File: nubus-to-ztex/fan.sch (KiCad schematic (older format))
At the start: 6 parts, among them J10 Conn_01x03_Male, J7 Conn_01x03_Male, J9 Conn_01x02

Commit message: large update
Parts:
- removed C33: 10uF, Capacitor_SMD:C_0805_2012Metric, symbol Device:C
- removed J10: Conn_01x03_Male, Connector_Molex:Molex_KK-254_AE-6410-03A_1x03_P2.54mm_Vertical, symbol Connector:Conn_01x03_Male
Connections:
- net labels removed: +12V
- wire segments 12 -> 8
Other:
- note removed: "12V Fan"
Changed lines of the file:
@@
 $Descr A4 11693 8268
 encoding utf-8
-Sheet 7 7
+Sheet 6 7
 Title "sbus-to-ztex blinkey stuff"
 Date ""
@@
 	6600 4500 6200 4500
 Connection ~ 6600 4400
-$Comp
-L Connector:Conn_01x03_Male J10
-U 1 1 61C52A59
-P 4400 5800
-F 0 "J10" H 4506 6078 50  0000 C CNN
-F 1 "Conn_01x03_Male" H 4506 5987 50  0000 C CNN
-F 2 "Connector_Molex:Molex_KK-254_AE-6410-03A_1x03_P2.54mm_Vertical" H 4400 5800 50  0001 C CNN
-F 3 "~" H 4400 5800 50  0001 C CNN
-F 4 "22-27-2031" H 4400 5800 50  0001 C CNN "MPN-ALT"
-F 5 "Molex" H 4400 5800 50  0001 C CNN "Manufacturer-ALT"
-F 6 "https://www.mouser.fr/ProductDetail/Molex/22-27-2031?qs=%2Fha2pyFadugXOaGYK9vaczm7nZ04txhJn3OGcnGWT3U=" H 4400 5800 50  0001 C CNN "URL-ALT"
-F 7 "640456-3" H 4400 5800 50  0001 C CNN "MPN"
-F 8 "TE Connectivity" H 4400 5800 50  0001 C CNN "Manufacturer"
-F 9 "https://www.lcsc.com/product-detail/Wire-To-Board-Wire-To-Wire-Connector_TE-Connectivity-640456-3_C86503.html" H 4400 5800 50  0001 C CNN "URL"
-	1    4400 5800
-	1    0    0    -1
-$EndComp
-$Comp
-L power:GND #PWR0208
-U 1 1 61C52A60
-P 4600 5700
-F 0 "#PWR0208" H 4600 5450 50  0001 C CNN
-F 1 "GND" V 4605 5572 50  0000 R CNN
-F 2 "" H 4600 5700 50  0001 C CNN
-F 3 "" H 4600 5700 50  0001 C CNN
-	1    4600 5700
-	0    -1   -1   0
-$EndComp
-$Comp
-L power:GND #PWR0209
-U 1 1 61C52A6C
-P 4600 5900
-F 0 "#PWR0209" H 4600 5650 50  0001 C CNN
-F 1 "GND" V 4605 5772 50  0000 R CNN
-F 2 "" H 4600 5900 50  0001 C CNN
-F 3 "" H 4600 5900 50  0001 C CNN
-	1    4600 5900
-	0    -1   -1   0
-$EndComp
-$Comp
-L Device:C C?
-U 1 1 61C52A73
-P 5150 5850
-AR Path="/5F69F4EF/61C52A73" Ref="C?"  Part="1"
-AR Path="/5F6B165A/61C52A73" Ref="C?"  Part="1"
-AR Path="/61B99D2C/61C52A73" Ref="C33"  Part="1"
-F 0 "C33" H 5175 5950 50  0000 L CNN
-F 1 "10uF" H 5175 5750 50  0000 L CNN
-F 2 "Capacitor_SMD:C_0805_2012Metric" H 5188 5700 50  0001 C CNN
-F 3 "" H 5150 5850 50  0000 C CNN
-F 4 "GRM21BR61E106MA73L" H 5150 5850 50  0001 C CNN "MPN"
-F 5 "https://lcsc.com/product-detail/Multilayer-Ceramic-Capacitors-MLCC-SMD-SMT_Murata-Electronics-GRM21BR61E106MA73L_C391262.html" H 5150 5850 50  0001 C CNN "URL"
-	1    5150 5850
-	1    0    0    -1
-$EndComp
-Wire Wire Line
-	4600 5800 5150 5800
-Wire Wire Line
-	5150 5800 5150 5700
-Wire Wire Line
-	4600 5900 5150 5900
-Wire Wire Line
-	5150 5900 5150 6000
-Connection ~ 4600 5900
-$Comp
-L power:+12V #PWR0210
-U 1 1 61C52B88
-P 4600 5800
-F 0 "#PWR0210" H 4600 5650 50  0001 C CNN
-F 1 "+12V" V 4615 5928 50  0000 L CNN
-F 2 "" H 4600 5800 50  0001 C CNN
-F 3 "" H 4600 5800 50  0001 C CNN
-	1    4600 5800
-	0    1    1    0
-$EndComp
-Connection ~ 4600 5800
 Text Notes 3950 4750 0    50   ~ 0
 5V Fan
-Text Notes 4000 5850 0    50   ~ 0
-12V Fan
 Text Notes 6800 4600 0    50   ~ 0
 3.3V access

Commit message: large clean-up update
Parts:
- renumbered C6 to C28, C31 to C29, J9 to J8
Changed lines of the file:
@@
 encoding utf-8
 Sheet 6 7
-Title "sbus-to-ztex blinkey stuff"
+Title "nubus-to-ztex extra conenctors (fan, ...)"
 Date ""
 Rev ""
@@
 $EndComp
 $Comp
-L power:GND #PWR0187
+L power:GND #PWR0107
 U 1 1 60E1EC2C
 P 4600 4650
-F 0 "#PWR0187" H 4600 4400 50  0001 C CNN
+F 0 "#PWR0107" H 4600 4400 50  0001 C CNN
 F 1 "GND" V 4605 4522 50  0000 R CNN
 F 2 "" H 4600 4650 50  0001 C CNN
@@
 $EndComp
 $Comp
-L power:+5V #PWR0188
+L power:+5V #PWR0108
 U 1 1 60E1ED6C
 P 4600 4750
-F 0 "#PWR0188" H 4600 4600 50  0001 C CNN
+F 0 "#PWR0108" H 4600 4600 50  0001 C CNN
 F 1 "+5V" V 4615 4878 50  0000 L CNN
 F 2 "" H 4600 4750 50  0001 C CNN
@@
 $EndComp
 $Comp
-L power:GND #PWR0189
+L power:GND #PWR0109
 U 1 1 60E1FA97
 P 4600 4850
-F 0 "#PWR0189" H 4600 4600 50  0001 C CNN
+F 0 "#PWR0109" H 4600 4600 50  0001 C CNN
 F 1 "GND" V 4605 4722 50  0000 R CNN
 F 2 "" H 4600 4850 50  0001 C CNN
@@
 P 5150 4800
 AR Path="/5F69F4EF/60E24715" Ref="C?"  Part="1"
-AR Path="/5F6B165A/60E24715" Ref="C6"  Part="1"
-AR Path="/61B99D2C/60E24715" Ref="C20"  Part="1"
-F 0 "C20" H 5175 4900 50  0000 L CNN
+AR Path="/5F6B165A/60E24715" Ref="C?"  Part="1"
+AR Path="/61B99D2C/60E24715" Ref="C28"  Part="1"
+F 0 "C28" H 5175 4900 50  0000 L CNN
 F 1 "47uF 10V+" H 5175 4700 50  0000 L CNN
 F 2 "Capacitor_SMD:C_0805_2012Metric" H 5188 4650 50  0001 C CNN
@@
 Connection ~ 4600 4850
 $Comp
-L Connector_Generic:Conn_01x02 J9
+L Connector_Generic:Conn_01x02 J8
 U 1 1 61BEF34E
 P 6800 4300
-F 0 "J9" H 6880 4292 50  0000 L CNN
+F 0 "J8" H 6880 4292 50  0000 L CNN
 F 1 "Conn_01x02" H 6880 4201 50  0000 L CNN
 F 2 "For_SeeedStudio:PinSocket_1x02_P2.54mm_Vertical_for_SeeedStudio" H 6800 4300 50  0001 C CNN
@@
 $EndComp
 $Comp
-L power:+3V3 #PWR0102
+L power:+3V3 #PWR0110
 U 1 1 61BEF445
 P 6600 4300
-F 0 "#PWR0102" H 6600 4150 50  0001 C CNN
+F 0 "#PWR0110" H 6600 4150 50  0001 C CNN
 F 1 "+3V3" V 6615 4428 50  0000 L CNN
 F 2 "" H 6600 4300 50  0001 C CNN
@@
 $EndComp
 $Comp
-L power:GND #PWR0200
+L power:GND #PWR0111
 U 1 1 61BEF4B8
 P 6600 4400
-F 0 "#PWR0200" H 6600 4150 50  0001 C CNN
+F 0 "#PWR0111" H 6600 4150 50  0001 C CNN
 F 1 "GND" V 6605 4272 50  0000 R CNN
 F 2 "" H 6600 4400 50  0001 C CNN
@@
 AR Path="/5F69F4EF/61C19258" Ref="C?"  Part="1"
 AR Path="/5F6B165A/61C19258" Ref="C?"  Part="1"
-AR Path="/61B99D2C/61C19258" Ref="C31"  Part="1"
-F 0 "C31" H 6225 4450 50  0000 L CNN
+AR Path="/61B99D2C/61C19258" Ref="C29"  Part="1"
+F 0 "C29" H 6225 4450 50  0000 L CNN
 F 1 "47uF 10V+" H 6225 4250 50  0000 L CNN
 F 2 "Capacitor_SMD:C_0805_2012Metric" H 6238 4200 50  0001 C CNN

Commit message: cut down brightness of LEDs, more 2x32 pin headers reference
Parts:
- removed C29: 47uF 10V+, Capacitor_SMD:C_0805_2012Metric, symbol Device:C
- removed J8: Conn_01x02, For_SeeedStudio:PinSocket_1x02_P2.54mm_Vertical_for_SeeedStudio, symbol Connector_Generic:Conn_01x02
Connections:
- net labels removed: +3V3
- wire segments 8 -> 4
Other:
- note removed: "3.3V access"
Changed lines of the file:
@@
 $Descr A4 11693 8268
 encoding utf-8
-Sheet 6 9
+Sheet 6 10
 Title "nubus-to-ztex extra conenctors (fan, ...)"
 Date ""
@@
 	5150 4850 5150 4950
 Connection ~ 4600 4850
-$Comp
-L Connector_Generic:Conn_01x02 J8
-U 1 1 61BEF34E
-P 6800 4300
-F 0 "J8" H 6880 4292 50  0000 L CNN
-F 1 "Conn_01x02" H 6880 4201 50  0000 L CNN
-F 2 "For_SeeedStudio:PinSocket_1x02_P2.54mm_Vertical_for_SeeedStudio" H 6800 4300 50  0001 C CNN
-F 3 "~" H 6800 4300 50  0001 C CNN
-F 4 "PM254V-11-02-H85" H 6800 4300 50  0001 C CNN "MPN"
-F 5 "https://www.lcsc.com/product-detail/Pin-Header-Female-Header_XFCN-PM254V-11-02-H85_C541849.html" H 6800 4300 50  0001 C CNN "URL"
-	1    6800 4300
-	1    0    0    -1
-$EndComp
-$Comp
-L power:+3V3 #PWR0110
-U 1 1 61BEF445
-P 6600 4300
-F 0 "#PWR0110" H 6600 4150 50  0001 C CNN
-F 1 "+3V3" V 6615 4428 50  0000 L CNN
-F 2 "" H 6600 4300 50  0001 C CNN
-F 3 "" H 6600 4300 50  0001 C CNN
-	1    6600 4300
-	0    -1   -1   0
-$EndComp
-$Comp
-L power:GND #PWR0111
-U 1 1 61BEF4B8
-P 6600 4400
-F 0 "#PWR0111" H 6600 4150 50  0001 C CNN
-F 1 "GND" V 6605 4272 50  0000 R CNN
-F 2 "" H 6600 4400 50  0001 C CNN
-F 3 "" H 6600 4400 50  0001 C CNN
-	1    6600 4400
-	0    1    1    0
-$EndComp
-$Comp
-L Device:C C?
-U 1 1 61C19258
-P 6200 4350
-AR Path="/5F69F4EF/61C19258" Ref="C?"  Part="1"
-AR Path="/5F6B165A/61C19258" Ref="C?"  Part="1"
-AR Path="/61B99D2C/61C19258" Ref="C29"  Part="1"
-F 0 "C29" H 6225 4450 50  0000 L CNN
-F 1 "47uF 10V+" H 6225 4250 50  0000 L CNN
-F 2 "Capacitor_SMD:C_0805_2012Metric" H 6238 4200 50  0001 C CNN
-F 3 "" H 6200 4350 50  0000 C CNN
-F 4 "C2012X5R1A476MTJ00E" H 6200 4350 50  0001 C CNN "MPN"
-F 5 "https://lcsc.com/product-detail/Multilayer-Ceramic-Capacitors-MLCC-SMD-SMT_TDK-C2012X5R1A476MTJ00E_C76636.html" H 6200 4350 50  0001 C CNN "URL"
-	1    6200 4350
-	1    0    0    -1
-$EndComp
-Wire Wire Line
-	6200 4200 6600 4200
-Wire Wire Line
-	6600 4200 6600 4300
-Connection ~ 6600 4300
-Wire Wire Line
-	6600 4400 6600 4500
-Wire Wire Line
-	6600 4500 6200 4500
-Connection ~ 6600 4400
 Text Notes 3950 4750 0    50   ~ 0
 5V Fan
-Text Notes 6800 4600 0    50   ~ 0
-3.3V access
 $EndSCHEMATC

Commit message: merge pmod & leds into an extended pmod on the outside. Also some BoM updates.
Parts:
- C28: MPN C2012X5R1A476MTJ00E -> GRM21BR61A476ME15K; MPN-ALT (none) -> C2012X5R1A476MTJ00E; URL https://lcsc.com/product-detail/Multilayer-Ceramic-Capacito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 -> https://www.lcsc.com/product-detail/Multilayer-Ceramic-Capa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; URL-ALT (none) -> https://lcsc.com/product-detail/Multilayer-Ceramic-Capacito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
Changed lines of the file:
@@
 $Descr A4 11693 8268
 encoding utf-8
-Sheet 6 10
+Sheet 6 9
 Title "nubus-to-ztex extra conenctors (fan, ...)"
 Date ""
@@
 F 2 "Capacitor_SMD:C_0805_2012Metric" H 5188 4650 50  0001 C CNN
 F 3 "" H 5150 4800 50  0000 C CNN
-F 4 "C2012X5R1A476MTJ00E" H 5150 4800 50  0001 C CNN "MPN"
-F 5 "https://lcsc.com/product-detail/Multilayer-Ceramic-Capacitors-MLCC-SMD-SMT_TDK-C2012X5R1A476MTJ00E_C76636.html" H 5150 4800 50  0001 C CNN "URL"
+F 4 "C2012X5R1A476MTJ00E" H 5150 4800 50  0001 C CNN "MPN-ALT"
+F 5 "https://lcsc.com/product-detail/Multilayer-Ceramic-Capacitors-MLCC-SMD-SMT_TDK-C2012X5R1A476MTJ00E_C76636.html" H 5150 4800 50  0001 C CNN "URL-ALT"
+F 6 "GRM21BR61A476ME15K" H 5150 4800 50  0001 C CNN "MPN"
+F 7 "https://www.lcsc.com/product-detail/Multilayer-Ceramic-Capacitors-MLCC-SMD-SMT_Murata-Electronics-GRM21BR61A476ME15K_C2292827.html" H 5150 4800 50  0001 C CNN "URL"
 	1    5150 4800
 	1    0    0    -1

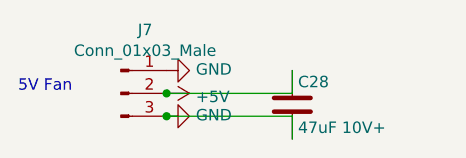
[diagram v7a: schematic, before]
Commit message: more update to V1.2 to try to limit cost
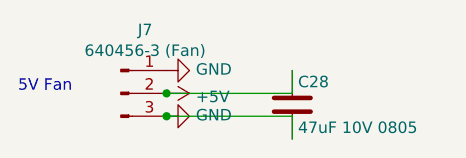
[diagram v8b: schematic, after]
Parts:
- C28: value 47uF 10V+ -> 47uF 10V 0805
- J7: value Conn_01x03_Male -> 640456-3 (Fan)
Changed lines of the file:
@@
 P 4400 4750
 F 0 "J7" H 4506 5028 50  0000 C CNN
-F 1 "Conn_01x03_Male" H 4506 4937 50  0000 C CNN
+F 1 "640456-3 (Fan)" H 4506 4937 50  0000 C CNN
 F 2 "Connector_Molex:Molex_KK-254_AE-6410-03A_1x03_P2.54mm_Vertical" H 4400 4750 50  0001 C CNN
 F 3 "~" H 4400 4750 50  0001 C CNN
@@
 AR Path="/61B99D2C/60E24715" Ref="C28"  Part="1"
 F 0 "C28" H 5175 4900 50  0000 L CNN
-F 1 "47uF 10V+" H 5175 4700 50  0000 L CNN
+F 1 "47uF 10V 0805" H 5175 4700 50  0000 L CNN
 F 2 "Capacitor_SMD:C_0805_2012Metric" H 5188 4650 50  0001 C CNN
 F 3 "" H 5150 4800 50  0000 C CNN
